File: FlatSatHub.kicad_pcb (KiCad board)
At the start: 4 copper layers, 166.3 x 166.3 mm, 39 parts, among them J1 Jack-DC, J10 DB26_Male_HighDensity_Mountin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, J11 Conn_02x02_Odd_Even, J12 DB26_Male_HighDensity_Mountin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, J13 Conn_02x02_Odd_Even, J14 DB26_Male_HighDensity_Mountin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, J15 Conn_02x02_Odd_Even, J16 DB26_Male_HighDensity_Mountin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, J17 Conn_02x02_Odd_Even, J2 DB26_Male_HighDensity_Mountin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

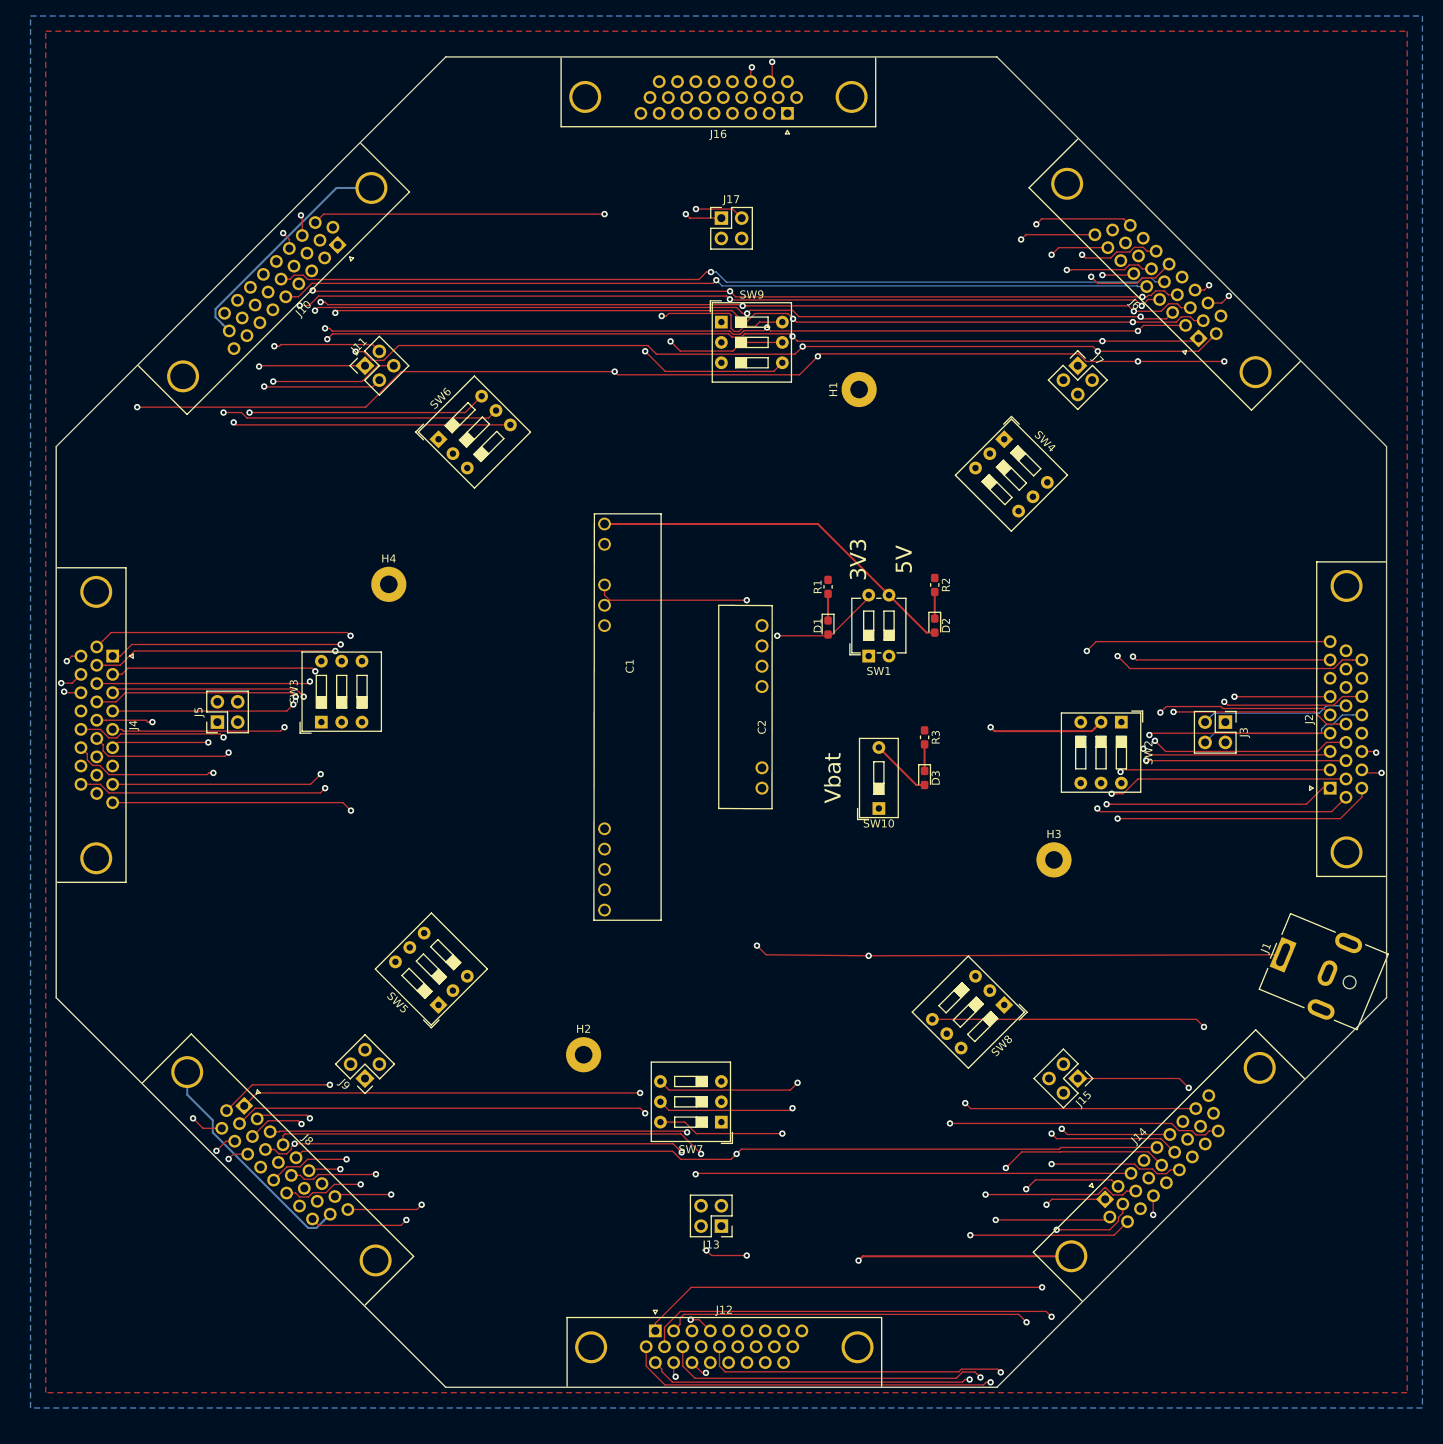
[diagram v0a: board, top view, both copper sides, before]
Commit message: Change DB-26-HD footprint to match what we want
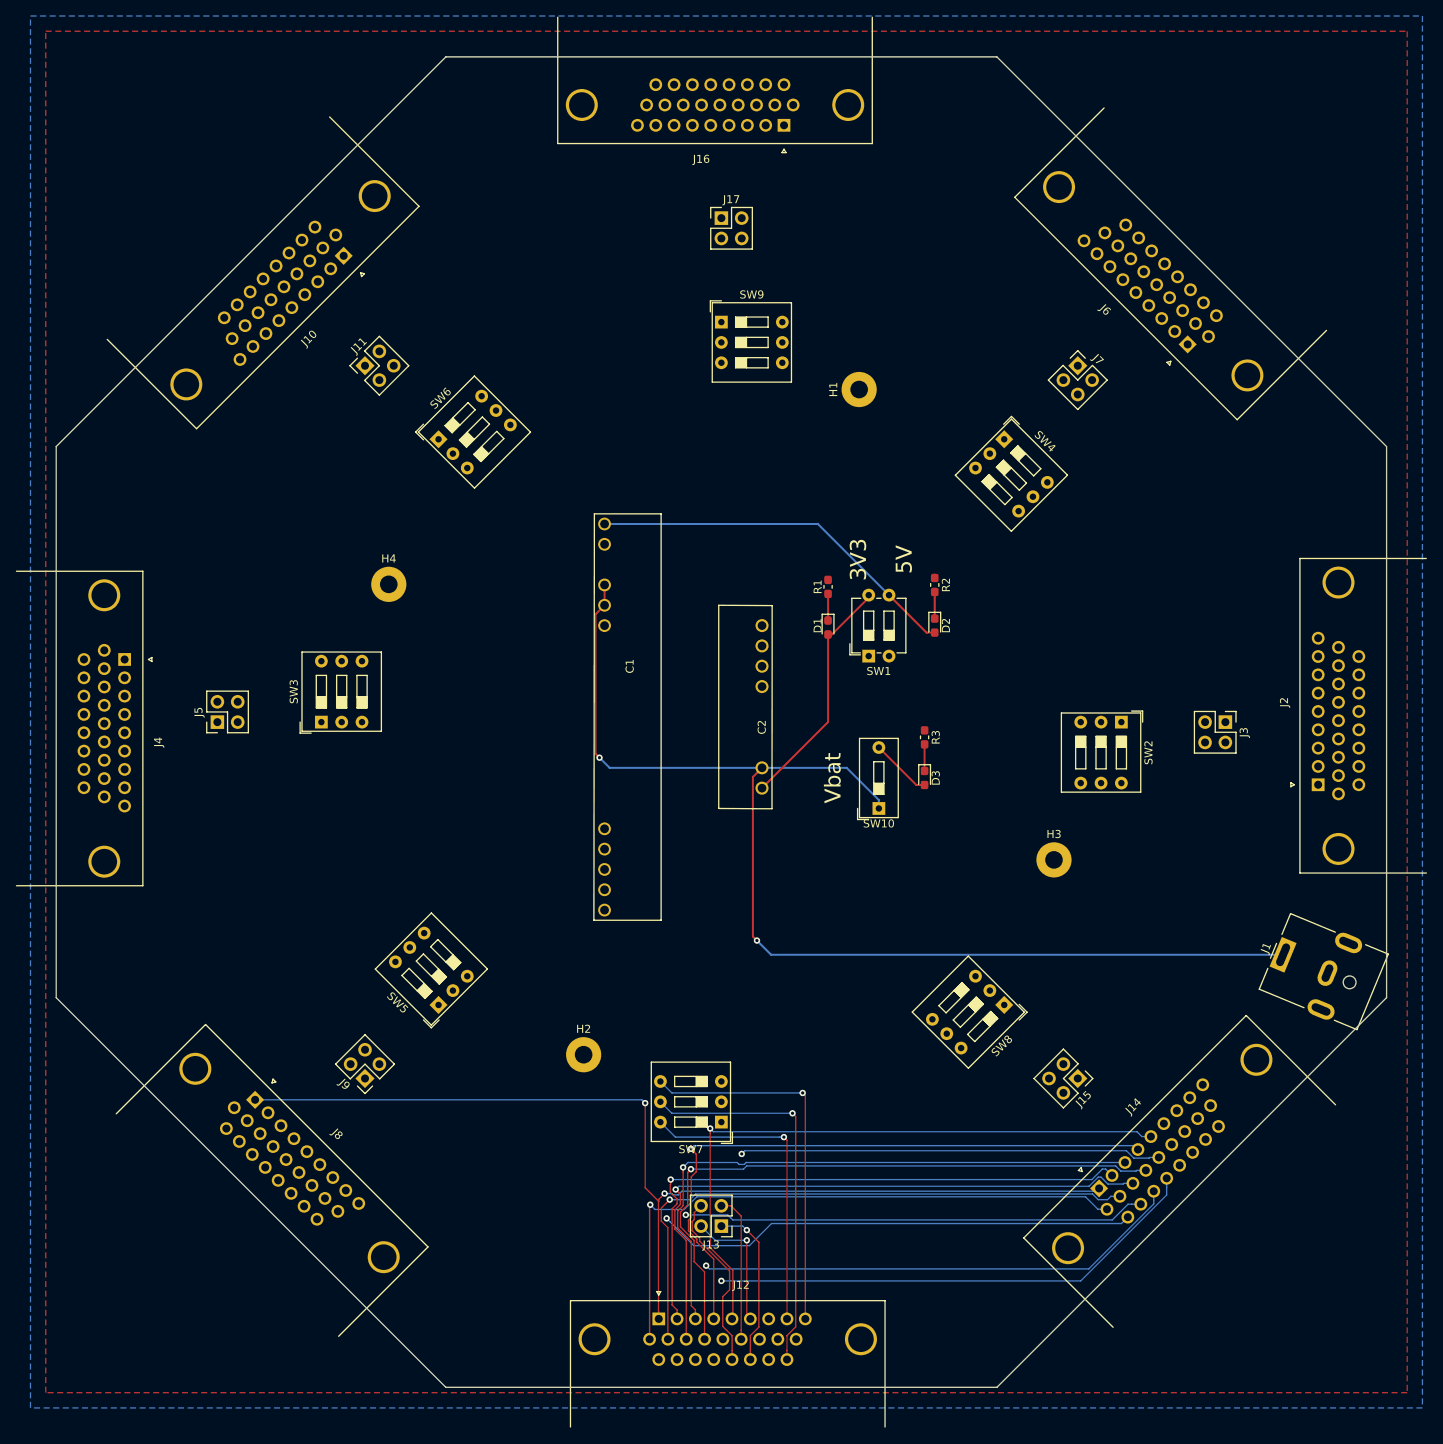
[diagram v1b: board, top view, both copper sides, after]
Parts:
- D1, D2: value GREEN LED -> LED
- D3: value GREEN_LED -> LED
- J10, J12, J14, J16, J2, J4, J6, J8: footprint DB-HD-26:DSUB-26-HD_Male_Horizontal_P2.29x1.98mm_EdgePinOffset3.03mm_Housed_MountingHolesOffset4.94mm_custom -> DB-HD-26:DSUB-26-HD_Male_Horizontal_P2.29x1.98mm_EdgePinOffset8.35mm_Housed_MountingHolesOffset10.89mm
- moved J6 8.55 mm to (153.0, 54.5)
- moved J10 8.55 mm to (47.6, 43.4)
- moved J14 8.55 mm to (142.0, 159.9)
- moved J8 8.55 mm to (36.5, 148.8)
- moved J16 8.55 mm to (102.6, 27.1)
- moved J4 8.55 mm to (20.2, 93.8)
- moved J12 8.55 mm to (86.9, 176.2)
- moved J2 8.55 mm to (169.3, 109.5)
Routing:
- net /I2C1_SCL: track 565.4 -> 78.7 mm, vias 11 -> 1
- net /I2C1_SDA: track 523.1 -> 75.5 mm, vias 8 -> 1
- net /SPI1_SCK: track 522.1 -> 75.3 mm, vias 8 -> 1
- net /SPI1_MOSI: track 503.3 -> 78.0 mm, vias 8 -> 1
- net /I2C2_SCL: track 500.5 -> 76.5 mm, vias 7 -> 1
- net /SPI4_SCK: track 489.6 -> 73.4 mm, vias 8 -> 1
- net /CAN1_RX: track 493.1 -> 77.0 mm, vias 5 -> 1
- net /SPI1_MISO: track 488.7 -> 74.4 mm, vias 8 -> 1
- net /SPI4_MOSI: track 482.7 -> 72.6 mm, vias 0 -> 1
- net /SPI4_MISO: track 488.6 -> 80.4 mm, vias 7 -> 1
- net /SPI1_SS: track 481.4 -> 75.8 mm, vias 7 -> 1
- net /SPI4_SS: track 474.1 -> 79.5 mm, vias 7 -> 1
- net /CAN1_TX: track 470.8 -> 80.5 mm, vias 4 -> 1
- net /I2C2_SDA: track 509.5 -> 132.6 mm, vias 8 -> 2
- net GND: track 112.4 -> 0.00 mm, vias 1 -> 0
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
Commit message: Rewire with new footprints
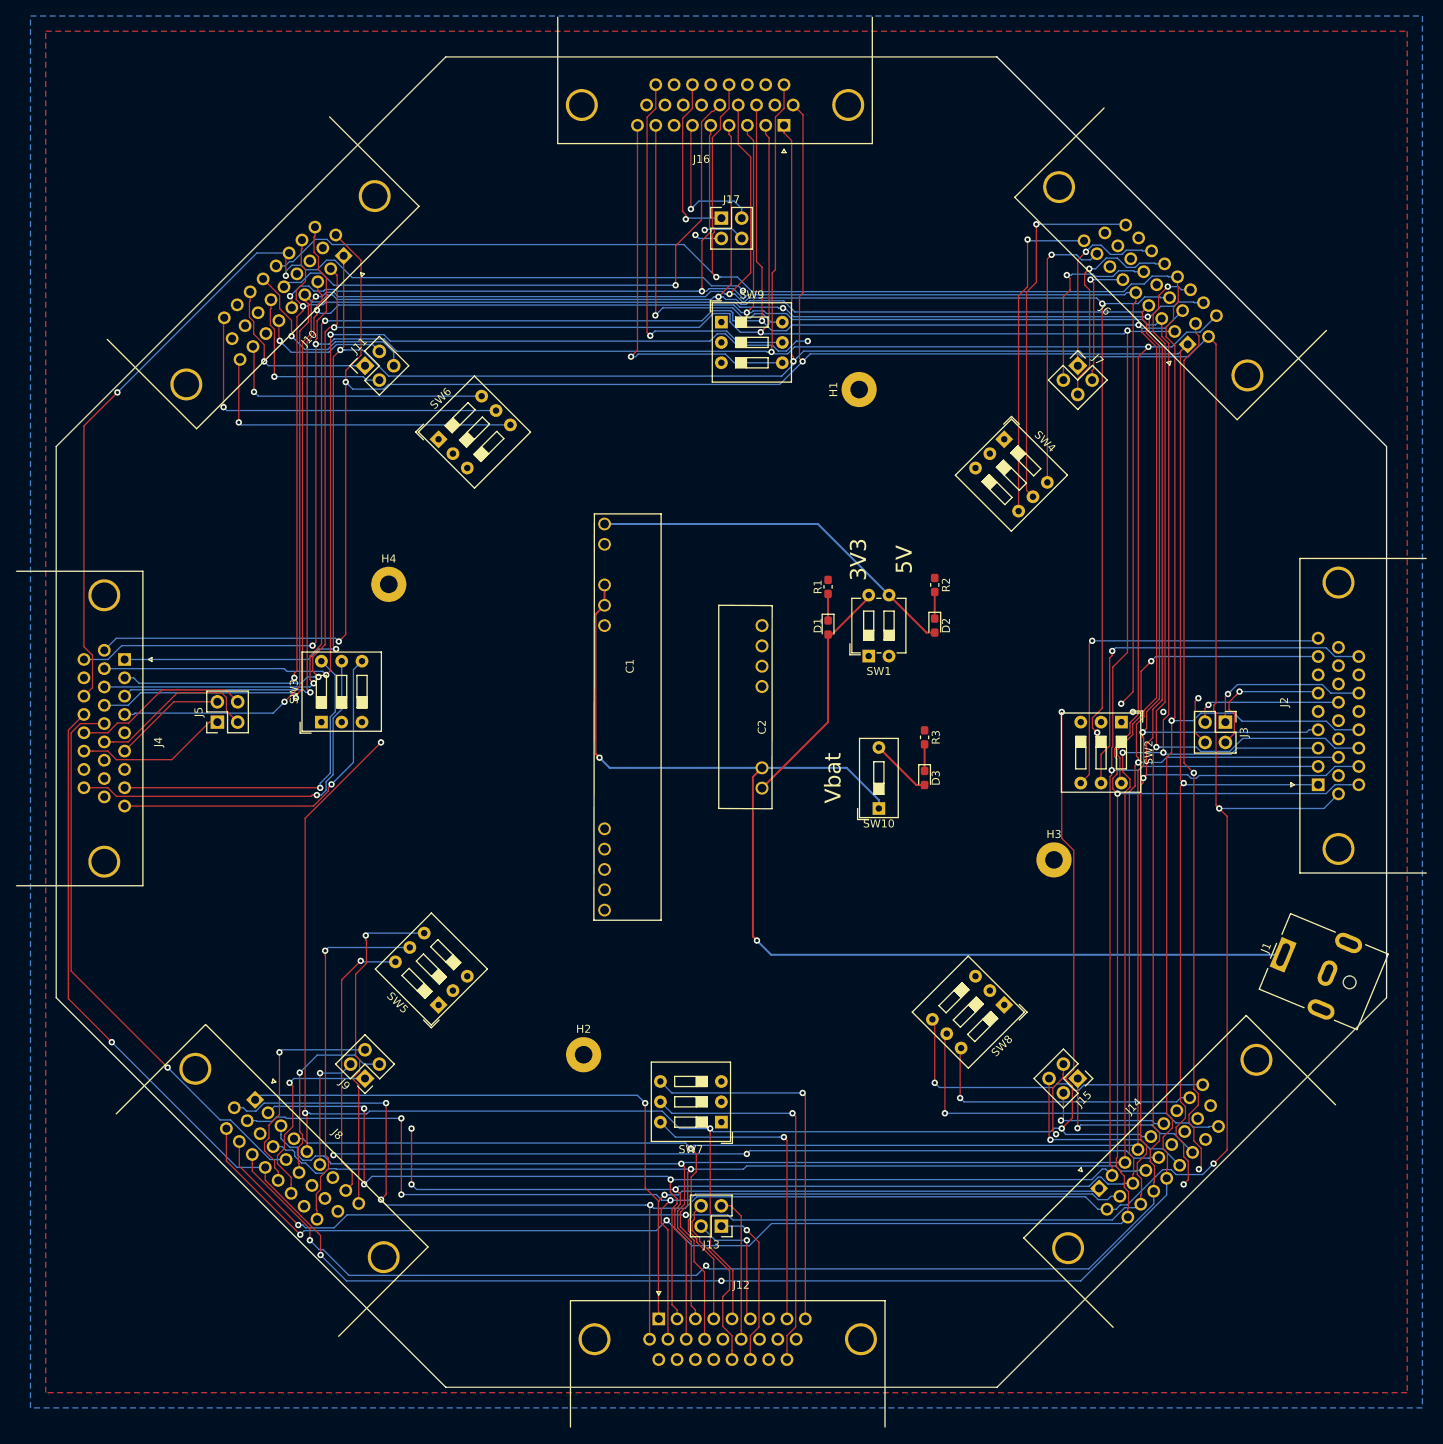
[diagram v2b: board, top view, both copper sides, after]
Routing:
- net /I2C1_SCL: track 78.7 -> 517.2 mm, vias 1 -> 7
- net /I2C2_SCL: track 76.5 -> 507.6 mm, vias 1 -> 7
- net /I2C1_SDA: track 75.5 -> 505.8 mm, vias 1 -> 8
- net /SPI1_SCK: track 75.3 -> 503.5 mm, vias 1 -> 8
- net /SPI4_SCK: track 73.4 -> 498.7 mm, vias 1 -> 7
- net /SPI4_MOSI: track 72.6 -> 490.4 mm, vias 1 -> 5
- net /SPI1_MOSI: track 78.0 -> 492.1 mm, vias 1 -> 8
- net /CAN1_TX: track 80.5 -> 490.0 mm, vias 1 -> 8
- net /SPI1_MISO: track 74.4 -> 480.0 mm, vias 1 -> 8
- net /CAN1_RX: track 77.0 -> 479.6 mm, vias 1 -> 6
- net /SPI1_SS: track 75.8 -> 470.0 mm, vias 1 -> 6
- net /SPI4_SS: track 79.5 -> 463.0 mm, vias 1 -> 4
- net /SPI4_MISO: track 80.4 -> 434.2 mm, vias 1 -> 6
- net /I2C2_SDA: track 132.6 -> 485.1 mm, vias 2 -> 7
- net /sheet5F237BCF/bus_3v3: track 0.00 -> 49.3 mm, vias 0 -> 1
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
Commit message: fix wiring and add serigraphy
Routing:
- net /SPI4_MISO: track 434.2 -> 489.0 mm, vias 6 -> 7
- net GND: track 0.00 -> 52.5 mm
- net 3V3: track 0.00 -> 47.9 mm, vias 0 -> 1
- net 5V: track 0.00 -> 44.2 mm, vias 0 -> 1
- net /SPI1_SS: track 470.0 -> 470.6 mm
